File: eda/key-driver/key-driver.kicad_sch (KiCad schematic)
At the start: 49 parts, among them J1 Conn_01x03_Socket, J10 Screw_Terminal_01x02, J11 Screw_Terminal_01x02, J12 Screw_Terminal_01x02, J13 Screw_Terminal_01x02, J14 Screw_Terminal_01x02, J15 Screw_Terminal_01x02, J2 Conn_01x03_Socket, J3 Screw_Terminal_01x02, J5 Screw_Terminal_01x02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

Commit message: Improve key driver circuit (r3)
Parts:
- removed SW1: SW_DIP_x03, Button_Switch_THT:SW_DIP_SPSTx03_Slide_9.78x9.8mm_W7.62mm_P2.54mm, symbol Switch:SW_DIP_x03
- added JP1, JP2, JP3: Jumper_2_Small_Open, self-playing-piano:PinHeader_1x02_P2.54mm_Vertical, symbol Jumper:Jumper_2_Small_Open
- D1, D10, D11, D2, D3, D4, D5, D6, D7, D8, D9: footprint Diode_THT:D_DO-201AD_P15.24mm_Horizontal -> Diode_THT:D_DO-201AE_P5.08mm_Vertical_KathodeUp
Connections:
- net GNDD: now also JP1.2 (B), JP2.2 (B), JP3.2 (B)
- net at A1.19 (A0): now also JP1.1 (A)
- net at A1.20 (A1): now also JP2.1 (A)
- net at A1.21 (A2): now also JP3.1 (A)

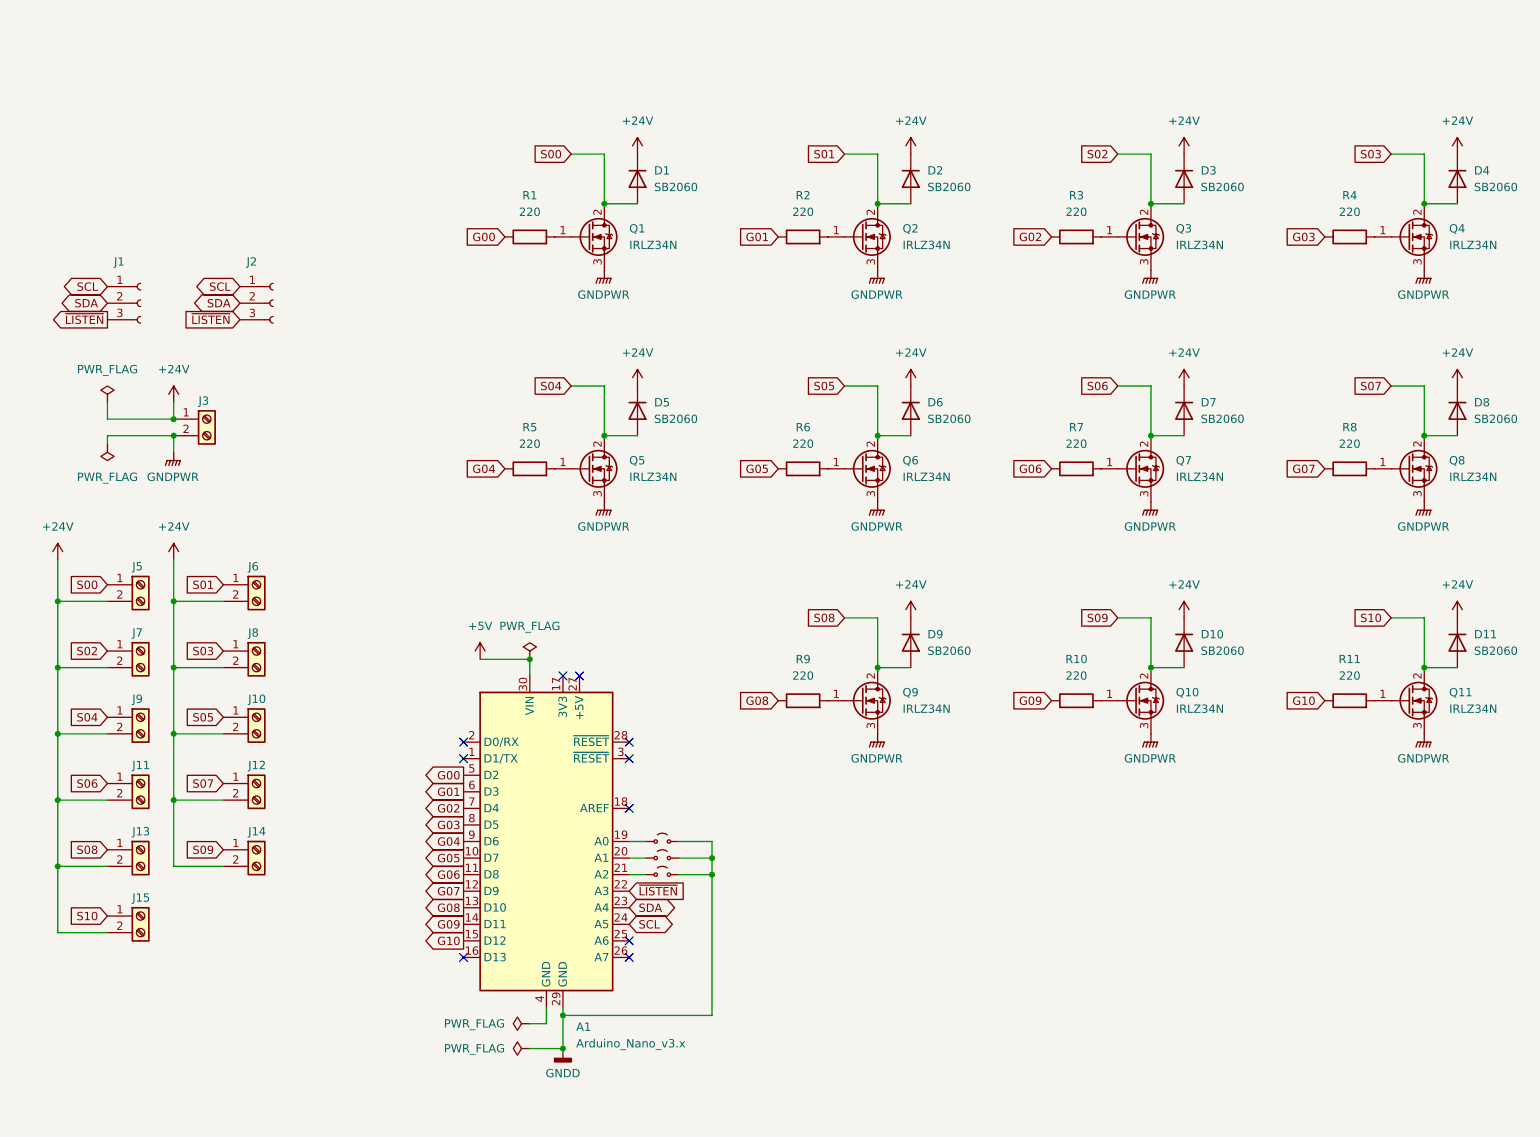
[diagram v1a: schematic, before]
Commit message: Modify key driver schematic and PCB to use new key arrangement, JST connectors, and wider traces
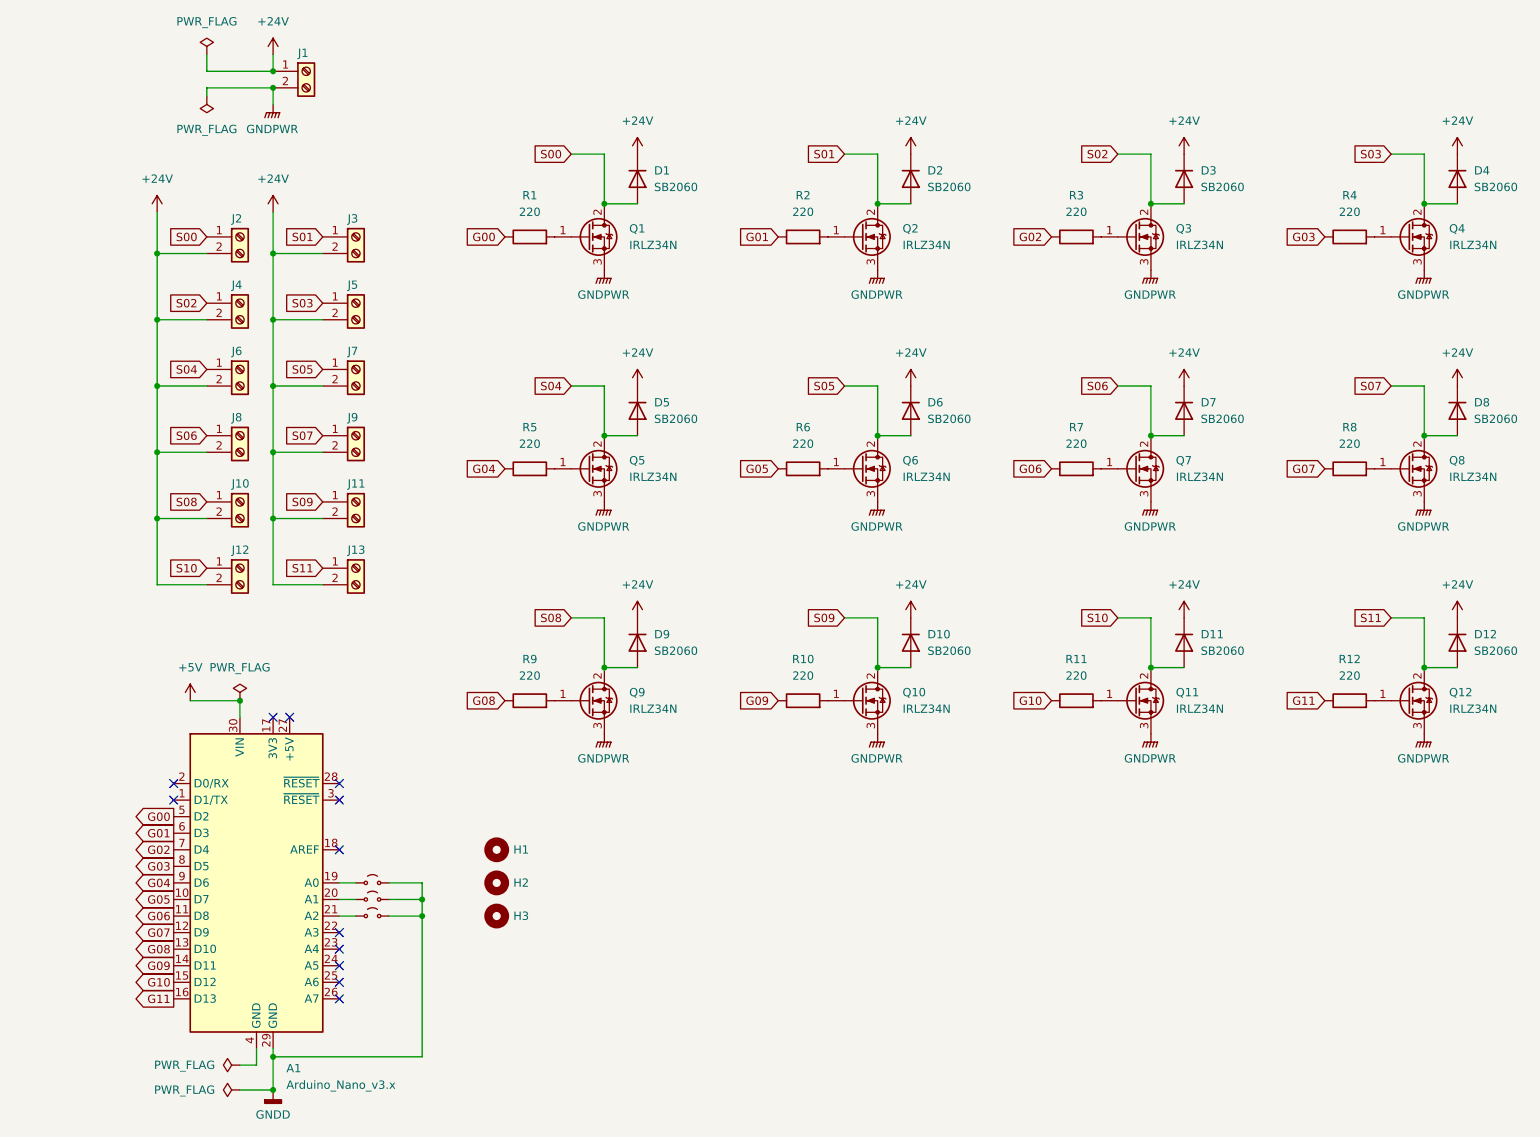
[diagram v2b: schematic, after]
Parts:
- removed J1, J2: Conn_01x03_Socket, self-playing-piano:PinSocket_1x03_P2.54mm_Vertical, symbol Connector:Conn_01x03_Socket
- added D12: SB2060, Diode_THT:D_DO-201AE_P5.08mm_Vertical_KathodeUp, symbol Device:D
- added H1, H2, H3: MountingHole, MountingHole:MountingHole_3.2mm_M3, symbol Mechanical:MountingHole
- added J13: Screw_Terminal_01x02, self-playing-piano:JST_EH_B2B-EH-A_1x02_P2.50mm_Vertical, symbol Connector:Screw_Terminal_01x02
- added Q12: IRLZ34N, self-playing-piano:TO-220-3_Vertical, symbol Transistor_FET:IRLZ34N
- added R12: 220, self-playing-piano:R_Axial_DIN0204_L3.6mm_D1.6mm_P7.62mm_Horizontal, symbol Device:R
- J1: renamed from J3; footprint self-playing-piano:TerminalBlock_TE_282834-2_1x02_P2.54mm_Horizontal -> self-playing-piano:JST_EH_B2B-EH-A_1x02_P2.50mm_Vertical
- J10: renamed from J13; footprint self-playing-piano:TerminalBlock_TE_282834-2_1x02_P2.54mm_Horizontal -> self-playing-piano:JST_EH_B2B-EH-A_1x02_P2.50mm_Vertical
- J11: renamed from J14; footprint self-playing-piano:TerminalBlock_TE_282834-2_1x02_P2.54mm_Horizontal -> self-playing-piano:JST_EH_B2B-EH-A_1x02_P2.50mm_Vertical
- J12: renamed from J15; footprint self-playing-piano:TerminalBlock_TE_282834-2_1x02_P2.54mm_Horizontal -> self-playing-piano:JST_EH_B2B-EH-A_1x02_P2.50mm_Vertical
- J2: renamed from J5; footprint self-playing-piano:TerminalBlock_TE_282834-2_1x02_P2.54mm_Horizontal -> self-playing-piano:JST_EH_B2B-EH-A_1x02_P2.50mm_Vertical
- J3: renamed from J6; footprint self-playing-piano:TerminalBlock_TE_282834-2_1x02_P2.54mm_Horizontal -> self-playing-piano:JST_EH_B2B-EH-A_1x02_P2.50mm_Vertical
- J4: renamed from J7; footprint self-playing-piano:TerminalBlock_TE_282834-2_1x02_P2.54mm_Horizontal -> self-playing-piano:JST_EH_B2B-EH-A_1x02_P2.50mm_Vertical
- J5: renamed from J8; footprint self-playing-piano:TerminalBlock_TE_282834-2_1x02_P2.54mm_Horizontal -> self-playing-piano:JST_EH_B2B-EH-A_1x02_P2.50mm_Vertical
- J6: renamed from J9; footprint self-playing-piano:TerminalBlock_TE_282834-2_1x02_P2.54mm_Horizontal -> self-playing-piano:JST_EH_B2B-EH-A_1x02_P2.50mm_Vertical
- J7: renamed from J10; footprint self-playing-piano:TerminalBlock_TE_282834-2_1x02_P2.54mm_Horizontal -> self-playing-piano:JST_EH_B2B-EH-A_1x02_P2.50mm_Vertical
- J8: renamed from J11; footprint self-playing-piano:TerminalBlock_TE_282834-2_1x02_P2.54mm_Horizontal -> self-playing-piano:JST_EH_B2B-EH-A_1x02_P2.50mm_Vertical
- J9: renamed from J12; footprint self-playing-piano:TerminalBlock_TE_282834-2_1x02_P2.54mm_Horizontal -> self-playing-piano:JST_EH_B2B-EH-A_1x02_P2.50mm_Vertical
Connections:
- net +24V: now also D12.1 (K), J13.2 (Pin_2)
- net GNDPWR: now also Q12.3 (S)
- net G11: now reaches A1.16 (D13)
- net G11: now also R12.1
- net SCL: no longer names the net of A1.24 (A5)
- net SDA: no longer names the net of A1.23 (A4)
- net ~{LISTEN}: no longer names the net of A1.22 (A3)
- new net: Q12.1 (G), R12.2
- new net S11: D12.2 (A), J13.1 (Pin_1), Q12.2 (D)
- no-connect marks 10 -> 12
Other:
- moved on the sheet: A1, D10, D11, D9, J1, J10, J11, J12, J2, J3, J4, J5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
